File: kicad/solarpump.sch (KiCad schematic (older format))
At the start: 1 part

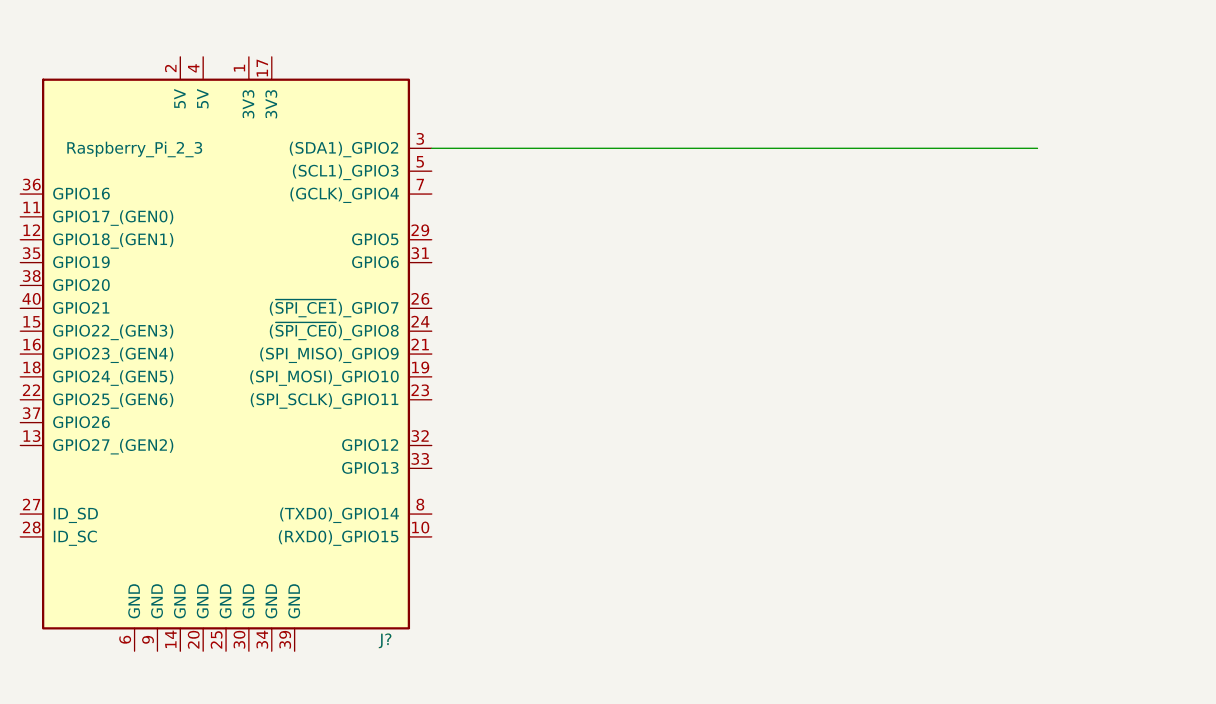
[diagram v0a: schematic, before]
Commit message: Update options and tests for servers
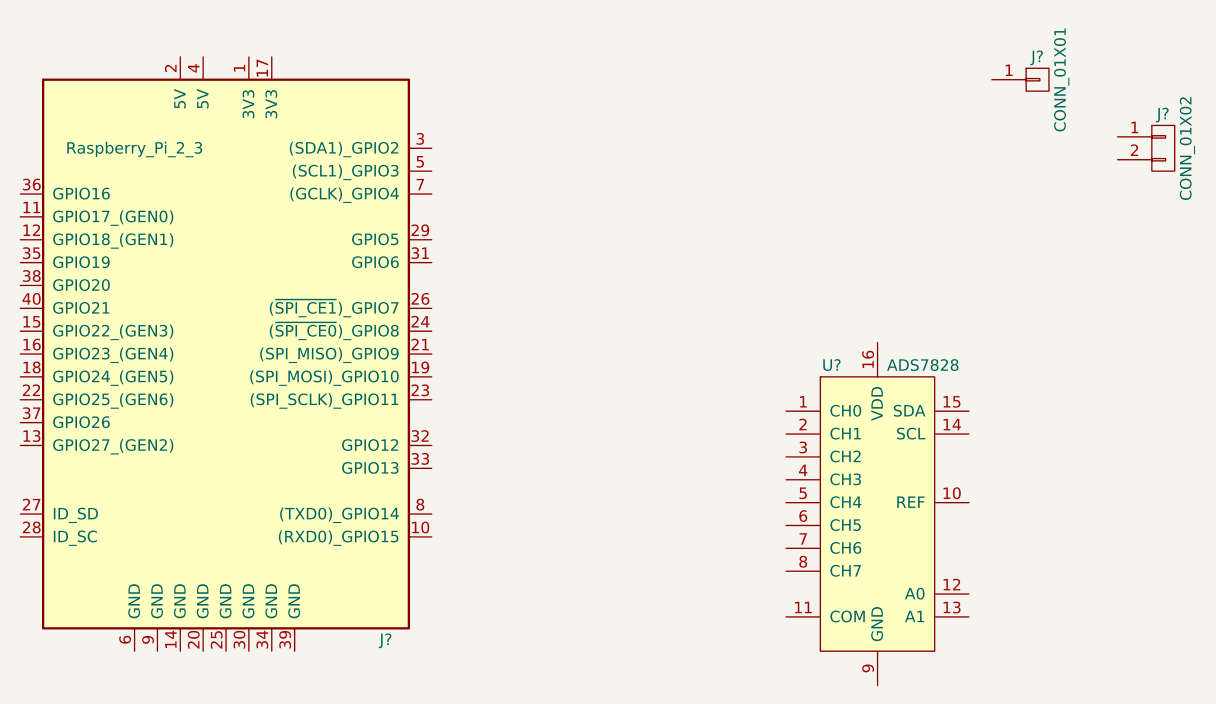
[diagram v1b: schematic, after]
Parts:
- added J?: CONN_01X01, symbol CONN_01X01
- added J?: CONN_01X02, symbol CONN_01X02
- added U?: ADS7828, Housings_SSOP:TSSOP-16_4.4x5mm_Pitch0.65mm, symbol ADS7828
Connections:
- wire segments 1 -> 0
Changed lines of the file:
@@
 LIBS:contrib
 LIBS:valves
+LIBS:solarpump-cache
 EELAYER 25 0
 EELAYER END
@@
 	1    0    0    -1
 $EndComp
-Wire Wire Line
-	3300 1650 5950 1650
+$Comp
+L ADS7828 U?
+U 1 1 5A610988
+P 5250 3200
+F 0 "U?" H 5050 3800 50  0000 C CNN
+F 1 "ADS7828" H 5450 3800 50  0000 C CNN
+F 2 "Housings_SSOP:TSSOP-16_4.4x5mm_Pitch0.65mm" H 6200 2500 50  0001 C CNN
+F 3 "" H 5250 3200 50  0001 C CNN
+	1    5250 3200
+	1    0    0    -1
+$EndComp
+$Comp
+L CONN_01X01 J?
+U 1 1 5A611033
+P 5950 1350
+F 0 "J?" H 5950 1450 50  0000 C CNN
+F 1 "CONN_01X01" V 6050 1350 50  0000 C CNN
+F 2 "" H 5950 1350 50  0001 C CNN
+F 3 "" H 5950 1350 50  0001 C CNN
+	1    5950 1350
+	1    0    0    -1
+$EndComp
+$Comp
+L CONN_01X02 J?
+U 1 1 5A6110DE
+P 6500 1650
+F 0 "J?" H 6500 1800 50  0000 C CNN
+F 1 "CONN_01X02" V 6600 1650 50  0000 C CNN
+F 2 "" H 6500 1650 50  0001 C CNN
+F 3 "" H 6500 1650 50  0001 C CNN
+	1    6500 1650
+	1    0    0    -1
+$EndComp
 $EndSCHEMATC
